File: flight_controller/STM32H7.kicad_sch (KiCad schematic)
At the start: 34 parts, among them J3 SM10B-SRSS-TB (LF)(SN), U1 STM32H743IIT6, U12 ESD7104MUTAG_C2987068, U13 ESD7104MUTAG_C2987068, X2 SC-32S32.768kHz20PPM7pF, X3 X322525MOB4SI

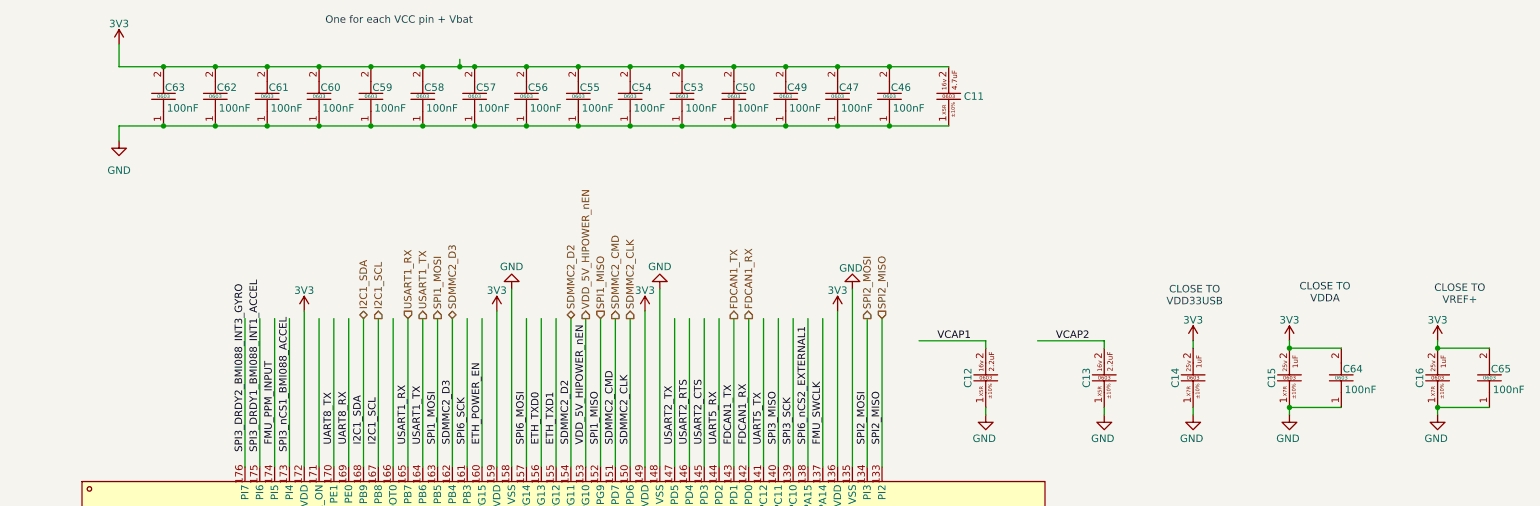
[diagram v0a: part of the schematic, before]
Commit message: updating symbols as in the shared library
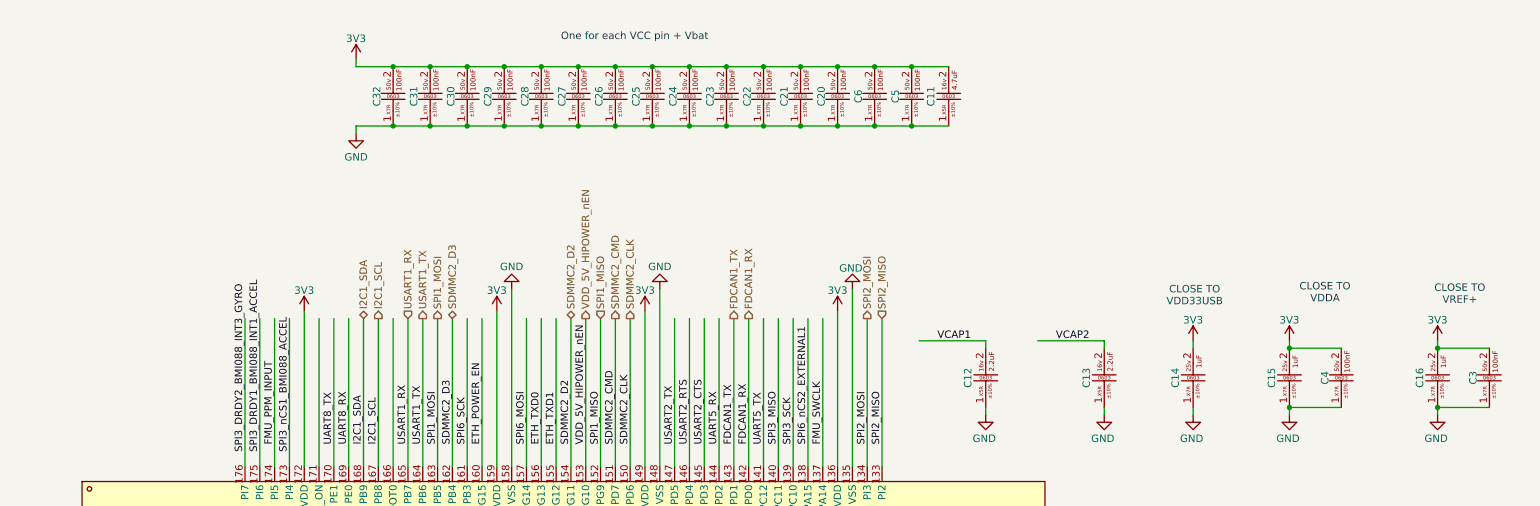
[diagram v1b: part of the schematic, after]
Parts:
- removed C46, C47, C49, C50, C53, C54, C55, C56, C57, C58, C59, C60, C61, C62, C63, C64, C65: CC0603KRX7R9BB104, easyeda2kicad:C0603, symbol easyeda2kicad:CC0603KRX7R9BB104
- added C20, C21, C22, C23, C24, C25, C26, C27, C28, C29, C3, C30, C31, C32, C4, C5, C6: CC0603KRX7R9BB104 (100nf , 0603 ,50v ,X7R), easyeda2kicad:C0603, symbol lampelKicadLIB:CC0603KRX7R9BB104 (100nf , 0603 ,50v ,X7R)
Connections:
- net 3V3: now also C20.2, C21.2, C22.2, C23.2, C24.2, C25.2, C26.2, C27.2, C28.2, C29.2, C3.2, C30.2, C31.2, C32.2, C4.2, C5.2, C6.2
- net GND: now also C20.1, C21.1, C22.1, C23.1, C24.1, C25.1, C26.1, C27.1, C28.1, C29.1, C3.1, C30.1, C31.1, C32.1, C4.1, C5.1, C6.1

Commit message: update debug conn
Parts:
- removed C10, C7: CL10C120JB8NNNC, easyeda2kicad:C0603, symbol easyeda2kicad:CL10C120JB8NNNC
- removed C8, C9: CC0402BRNPO9BN7R0, easyeda2kicad:C0402, symbol easyeda2kicad:CC0402BRNPO9BN7R0
- removed D1: BAS70-04_C7502687, easyeda2kicad:SOT-23-3_L2.9-W1.3-P1.90-LS2.4-BL-1, symbol easyeda2kicad:BAS70-04_C7502687
- removed J3: SM10B-SRSS-TB (LF)(SN), easyeda2kicad:CONN-SMD_10P-P1.00_SM10B-SRSS-TB-LF-SN, symbol easyeda2kicad:SM10B-SRSS-TB(LF)(SN)
- removed U12, U13: ESD7104MUTAG_C2987068, easyeda2kicad:DFN-10_L2.5-W1.0-P0.50-BL, symbol easyeda2kicad:ESD7104MUTAG_C2987068
- removed X2: SC-32S32.768kHz20PPM7pF, easyeda2kicad:OSC-SMD_L3.2-W1.5, symbol easyeda2kicad:SC-32S32.768kHz20PPM7pF
- removed X3: X322525MOB4SI, easyeda2kicad:CRYSTAL-SMD_4P-L3.2-W2.5-BL, symbol easyeda2kicad:X322525MOB4SI
- added C10, C9: 0603CG7R0C500NT (7pf , 0603 , 50v), easyeda2kicad:C0603, symbol lampelKicadLIB:0603CG7R0C500NT (7pf , 0603 , 50v)
- added C51, C52: CL10C120JB8NNNC ( 12pf , 0603 , 50v , C0G), easyeda2kicad:C0603, symbol lampelKicadLIB:CL10C120JB8NNNC ( 12pf , 0603 , 50v , C0G)
- added D10: KT-0603R, easyeda2kicad:LED0603-RD, symbol easyeda2kicad:KT-0603R
- added D3: 0603 Green 509-620mcd, easyeda2kicad:LED0603-RD, symbol easyeda2kicad:0603Green509-620mcd
- added R2, R5, R50: 603WAF1000T5E (100ohm , 0603), easyeda2kicad:R0603, symbol lampelKicadLIB:0603WAF1000T5E (100ohm , 0603)
- added SW2: 6.0*6.0*6.0, easyeda2kicad:SW-SMD_4P-L6.0-W6.0-P4.50-LS8.6, symbol easyeda2kicad:6.0*6.0*6.0
- added U6: HB-PH9-12727PB2GOB, easyeda2kicad:HDR-SMD_14P-P1.27-V-M-R2-C7-LS5.5, symbol easyeda2kicad:HB-PH9-12727PB2GOB
- added X1: SC-32S32.768kHz20PPM7pF, easyeda2kicad:OSC-SMD_L3.2-W1.5, symbol lampelKicadLIB:SC-32S32.768kHz20PPM7pF
- added X2: X322525MOB4SI, easyeda2kicad:CRYSTAL-SMD_4P-L3.2-W2.5-BL, symbol lampelKicadLIB:X322525MOB4SI
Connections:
- net 3V3: now also U6.3
- net GND: now also C10.1, C51.1, C52.1, C9.1, D10.1 (K), D3.1 (K), R2.2, SW2.3, SW2.4, U6.5, U6.7, X2.2 (GND), X2.4 (GND)
- net OSC32_IN: now also C9.2, X1.1
- net OSC32_OUT: now also C10.2, X1.2
- net OSC_IN: now also C52.2, X2.1 (OSC1)
- net OSC_OUT: now also C51.2, X2.3 (OSC2)
- net STM32H7_NRST: now also SW2.1, SW2.2
- net USART3_RX renamed UART3_VCP_RX
- net UART3_VCP_RX: now also U6.13
- net USART3_TX renamed UART3_VCP_TX
- net UART3_VCP_TX: now also U6.14
- new net: R2.1, U6.11
- new net: D10.2 (A), R50.1
- new net: D3.2 (A), R5.1
- new net LED1: R5.2
- new net LED2: R50.2
- new net SWCLK: U6.6
- new net SWDIO: U6.4
- new net SWO: U6.8
- no-connect marks 0 -> 5
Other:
- note added: "JTAG/SW CONN"
- note added: "LEDS"
- note added: "NRST has an internal pullup"
- note added: "Original part number for the stm32 v3 set is : FTSH-107-01-L-DV-K-A"

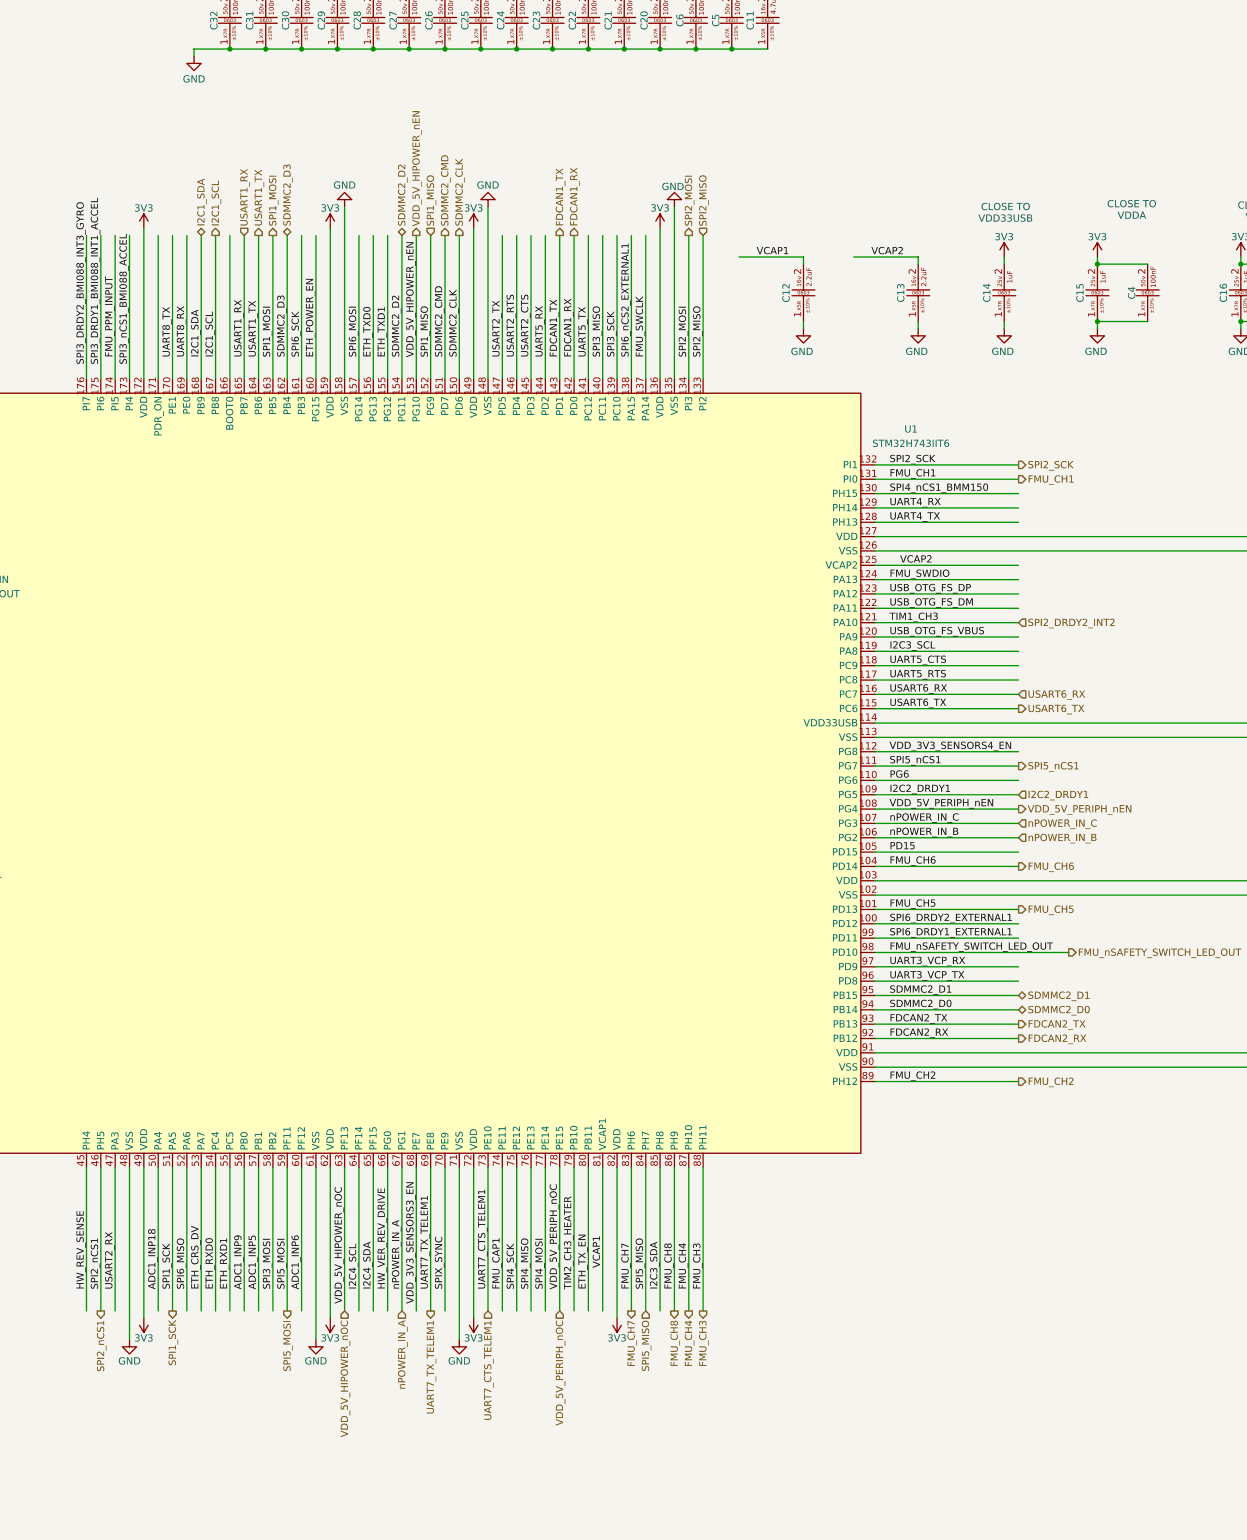
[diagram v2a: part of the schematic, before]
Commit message: gps and power blocks
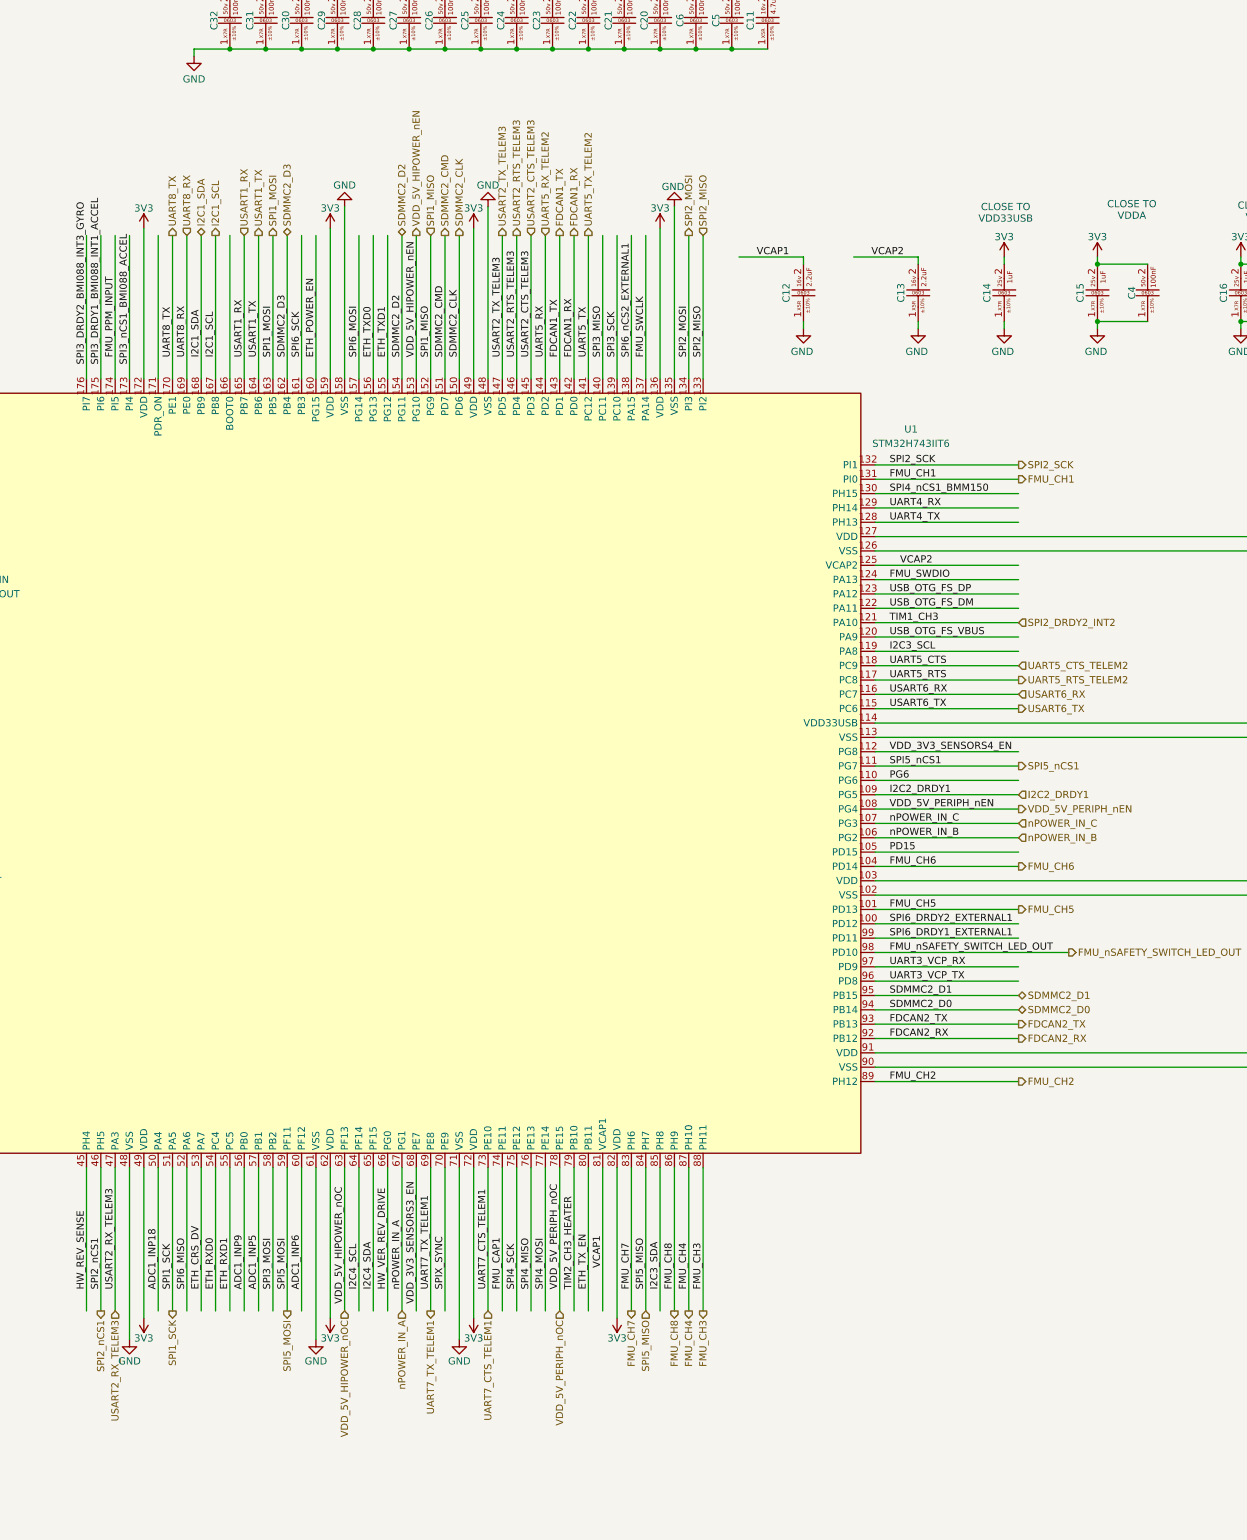
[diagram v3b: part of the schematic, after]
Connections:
- net UART5_CTS renamed UART5_CTS_TELEM2
- net UART5_RTS renamed UART5_RTS_TELEM2
- net UART5_RX renamed UART5_RX_TELEM2
- net UART5_TX renamed UART5_TX_TELEM2
- net USART2_CTS renamed USART2_CTS_TELEM3
- net USART2_RTS renamed USART2_RTS_TELEM3
- net USART2_RX renamed USART2_RX_TELEM3
- net USART2_TX renamed USART2_TX_TELEM3
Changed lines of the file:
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@@
 			(width 0)
 			(type default)
+			(color 255 0 0 1)
 		)
 	)
@@
 			(width 0)
 			(type default)
+			(color 255 0 0 1)
 		)
 	)
@@
 		)
 	)
-	(label "USART2_RTS"
+	(label "USART2_RTS_TELEM3"
 		(at 422.91 101.6 90)
 		(effects
@@
 		)
 	)
-	(label "USART2_TX"
+	(label "USART2_TX_TELEM3"
 		(at 420.37 101.6 90)
 		(effects
@@
 		)
 	)
-	(label "USART2_RX"
+	(label "USART2_RX_TELEM3"
 		(at 351.79 266.7 90)
 		(effects
@@
 		)
 	)
-	(label "USART2_CTS"
+	(label "USART2_CTS_TELEM3"
 		(at 425.45 101.6 90)
 		(effects
@@
 		)
 	)
+	(hierarchical_label "USART2_RX_TELEM3"
+		(shape input)
+		(at 351.79 270.51 270)
+		(effects
+			(font
+				(size 1.27 1.27)
+			)
+			(justify right)
+		)
+	)
 	(hierarchical_label "I2C2_SDA"
 		(shape bidirectional)
@@
 		)
 	)
+	(hierarchical_label "USART2_CTS_TELEM3"
+		(shape input)
+		(at 425.45 80.01 90)
+		(effects
+			(font
+				(size 1.27 1.27)
+			)
+			(justify left)
+		)
+	)
+	(hierarchical_label "UART8_TX"
+		(shape output)
+		(at 361.95 80.01 90)
+		(effects
+			(font
+				(size 1.27 1.27)
+			)
+			(justify left)
+		)
+	)
 	(hierarchical_label "SPI1_nCS1"
 		(shape output)
@@
 		)
 	)
+	(hierarchical_label "USART2_RTS_TELEM3"
+		(shape output)
+		(at 422.91 80.01 90)
+		(effects
+			(font
+				(size 1.27 1.27)
+			)
+			(justify left)
+		)
+	)
 	(hierarchical_label "SPI5_SCK"
 		(shape output)
@@
 			)
 			(justify right)
+		)
+	)
+	(hierarchical_label "UART5_TX_TELEM2"
+		(shape output)
+		(at 435.61 80.01 90)
+		(effects
+			(font
+				(size 1.27 1.27)
+			)
+			(justify left)
+		)
+	)
+	(hierarchical_label "UART5_CTS_TELEM2"
+		(shape input)
+		(at 511.81 156.21 0)
+		(effects
+			(font
+				(size 1.27 1.27)
+			)
+			(justify left)
 		)
 	)
@@
 		)
 	)
+	(hierarchical_label "USART2_TX_TELEM3"
+		(shape output)
+		(at 420.37 80.01 90)
+		(effects
+			(font
+				(size 1.27 1.27)
+			)
+			(justify left)
+		)
+	)
 	(hierarchical_label "VDD_5V_PERIPH_nEN"
 		(shape output)
@@
 		)
 	)
+	(hierarchical_label "UART5_RTS_TELEM2"
+		(shape output)
+		(at 511.81 158.75 0)
+		(effects
+			(font
+				(size 1.27 1.27)
+			)
+			(justify left)
+		)
+	)
 	(hierarchical_label "FMU_CH1"
 		(shape output)
@@
 		)
 	)
+	(hierarchical_label "UART5_RX_TELEM2"
+		(shape input)
+		(at 427.99 80.01 90)
+		(effects
+			(font
+				(size 1.27 1.27)
+			)
+			(justify left)
+		)
+	)
 	(hierarchical_label "VDD_5V_HIPOWER_nOC"
 		(shape input)
@@
 		)
 	)
+	(hierarchical_label "UART8_RX"
+		(shape input)
+		(at 364.49 80.01 90)
+		(effects
+			(font
+				(size 1.27 1.27)
+			)
+			(justify left)
+		)
+	)

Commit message: ALL CONNECTORS, ETH, SERVO,RC,SPI,FLASH and more. to finish GPSand STM32 PINOUT
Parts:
- added R66, R67, R68, R69, R70, R71, R73: 0603WAF1002T5E, easyeda2kicad:R0603, symbol easyeda2kicad:0603WAF1002T5E
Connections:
- net 3V3: now also R66.2, R67.2, R68.2, R69.2, R70.2, R71.2
- net GND: now also R73.1
- net I2C1_SCL: now also R68.1
- net I2C1_SDA: now also R69.1
- net I2C2_SCL: now also R66.1
- net I2C2_SDA: now also R67.1
- net I2C3_SCL: now also R70.1
- net I2C3_SDA: now also R71.1
- net BOOT0: now reaches U1.166 (BOOT0)
- net BOOT0: now also R73.2
- net FMU_CH5 renamed QUADSPI_BK1_IO3
- net I2C2_DRDY1: no longer names the net of U1.109 (PG5)
- net PG6 renamed QUADSPI_BK1_NCS
- net SPI6_DRDY1_EXTERNAL1 renamed QUADSPI_BK1_IO0
- net SPI6_DRDY2_EXTERNAL1 renamed QUADSPI_BK1_IO1
- net SPI6_nRESET_EXTERNAL1 renamed QUADSPI_CLK
- net TRACECLK renamed QUADSPI_BK1_IO2
- net UART3_VCP_RX renamed USART3_VCP_RX
- net UART3_VCP_TX renamed USART3_VCP_TX
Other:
- note added: "TIM4_CH3"
- note added: "TIM5_CH1"
- note added: "TIM5_CH2"
- note added: "TIM5_CH3"
- note added: "TIM5_CH4"
- note added: "was FMU_CH5"
- note added: "was SPI6_DRDY1_EXTERNAL1"
- note added: "was SPI6_DRDY2_EXTERNAL1"
- note added: "was SPI6_nRESET"
- note added: "was TRACECLK"

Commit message: cleanup and improvements
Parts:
- added R1, R6: 603WAF0000T5E (0ohm , 0603), easyeda2kicad:R0603, symbol lampelKicadLIB:0603WAF0000T5E (0ohm , 0603)
- added R27: FRC0603F4642TS (46.4kohm , 0603), easyeda2kicad:R0603, symbol lampelKicadLIB:FRC0603F4642TS (46.4kohm , 0603)
- added R28: 0603WAF8452T5E (84.5kohm , 0603), easyeda2kicad:R0603, symbol lampelKicadLIB:0603WAF8452T5E (84.5kohm , 0603)
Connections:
- net 3V3: now also R1.2, R28.2
- net HW_REV_SENSE: now also R27.2, R28.1
- net HW_VER_REV_DRIVE: now also R27.1, R6.1
- net HW_VER_SENSE: now also R1.1, R6.2
- net PD15 renamed SD_CARD_DETECT
- net SPI3_nCS1_BMI088_ACCEL renamed SPI3_nCS1
- net SWO: no longer names the net of U6.8
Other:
- note added: "Base board ver"
- note added: "FMU V6X board rev"
- note added: "R1"
- note added: "R2"
- note added: "SWO"
